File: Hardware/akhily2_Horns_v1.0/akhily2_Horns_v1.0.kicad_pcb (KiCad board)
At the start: 2 copper layers, 0 parts

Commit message: Save work before applying fixes
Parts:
- added C1: 0.1uF, Capacitor_THT:CP_Radial_D5.0mm_P2.00mm, F.Cu at (87.0, 75.0)
- added C2: 0.1uF, Capacitor_THT:CP_Radial_D5.0mm_P2.00mm, F.Cu at (99.0, 75.0)
- added C3: 0.1uF, Capacitor_THT:CP_Radial_D5.0mm_P2.00mm, F.Cu at (111.0, 75.0)
- added C4: 1uF, Capacitor_THT:CP_Radial_D5.0mm_P2.00mm, F.Cu at (123.0, 75.0)
- added C5: 1uF, Capacitor_THT:CP_Radial_D5.0mm_P2.00mm, F.Cu at (87.0, 90.0)
- added C6: 10uF, Capacitor_THT:CP_Radial_D5.0mm_P2.00mm, F.Cu at (99.0, 90.0)
- added C7: 10uF, Capacitor_THT:CP_Radial_D5.0mm_P2.00mm, F.Cu at (111.0, 90.0)
- added C8: 100uF, Capacitor_THT:CP_Radial_D5.0mm_P2.00mm, F.Cu at (123.0, 90.0)
- added C9: 0.1uF, Capacitor_THT:CP_Radial_D5.0mm_P2.00mm, F.Cu at (72.0, 87.0)
- added D1: ES2DA-13-F, Diode_THT:D_DO-41_SOD81_P10.16mm_Horizontal, F.Cu at (58.8, 100.5)
- added F1: 2A, Fuse:Fuseholder_Cylinder-5x20mm_Schurter_FAB_0031-355x_Horizontal_Closed, F.Cu at (62.0, 75.0)
- added J1: Conn_01x03, Connector_PinHeader_2.54mm:PinHeader_1x03_P2.54mm_Vertical, F.Cu at (33.5, 51.0)
- added J2: Conn_01x02, Connector_PinHeader_2.54mm:PinHeader_1x02_P2.54mm_Vertical, F.Cu at (33.5, 66.0)
- added J3: Conn_01x02, Connector_PinHeader_2.54mm:PinHeader_1x02_P2.54mm_Vertical, F.Cu at (33.5, 81.0)
- added J4: Conn_01x02, Connector_PinHeader_2.54mm:PinHeader_1x02_P2.54mm_Vertical, F.Cu at (33.5, 96.0)
- added Q1: Q_NMOS_GSD, Package_TO_SOT_SMD:TO-252-2, F.Cu at (62.0, 87.0)
- added R1: 1k, Resistor_THT:R_Axial_DIN0207_L6.3mm_D2.5mm_P10.16mm_Horizontal, F.Cu at (72.0, 75.0)
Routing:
- net +24V: track 0.00 -> 190.4 mm
- net Net-(Q1-D): track 0.00 -> 173.4 mm
- net GND: track 0.00 -> 120.3 mm
- net /HORN_CTL: track 0.00 -> 87.0 mm
- net /HORN_IN: track 0.00 -> 76.1 mm
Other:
- board outline added: 110 x 65 mm

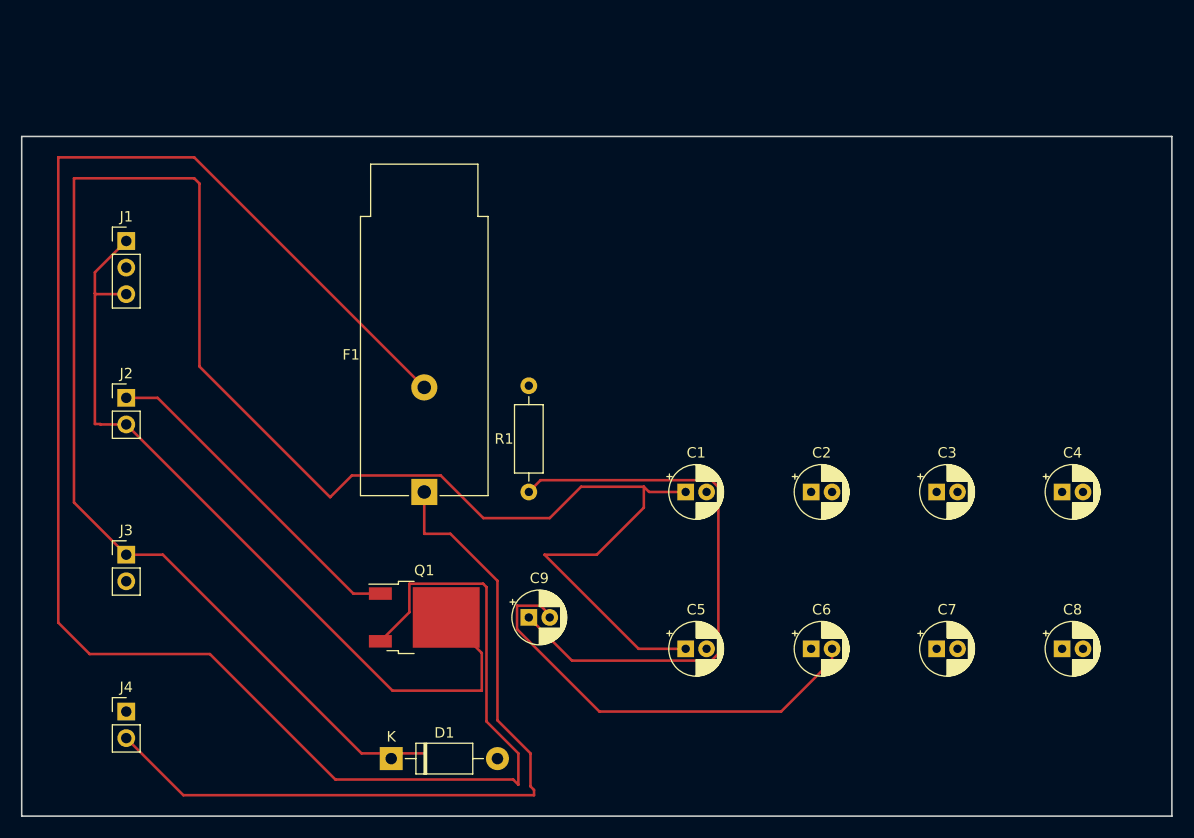
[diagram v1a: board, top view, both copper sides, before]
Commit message: Horns board specs, schematic, layout, gerbers
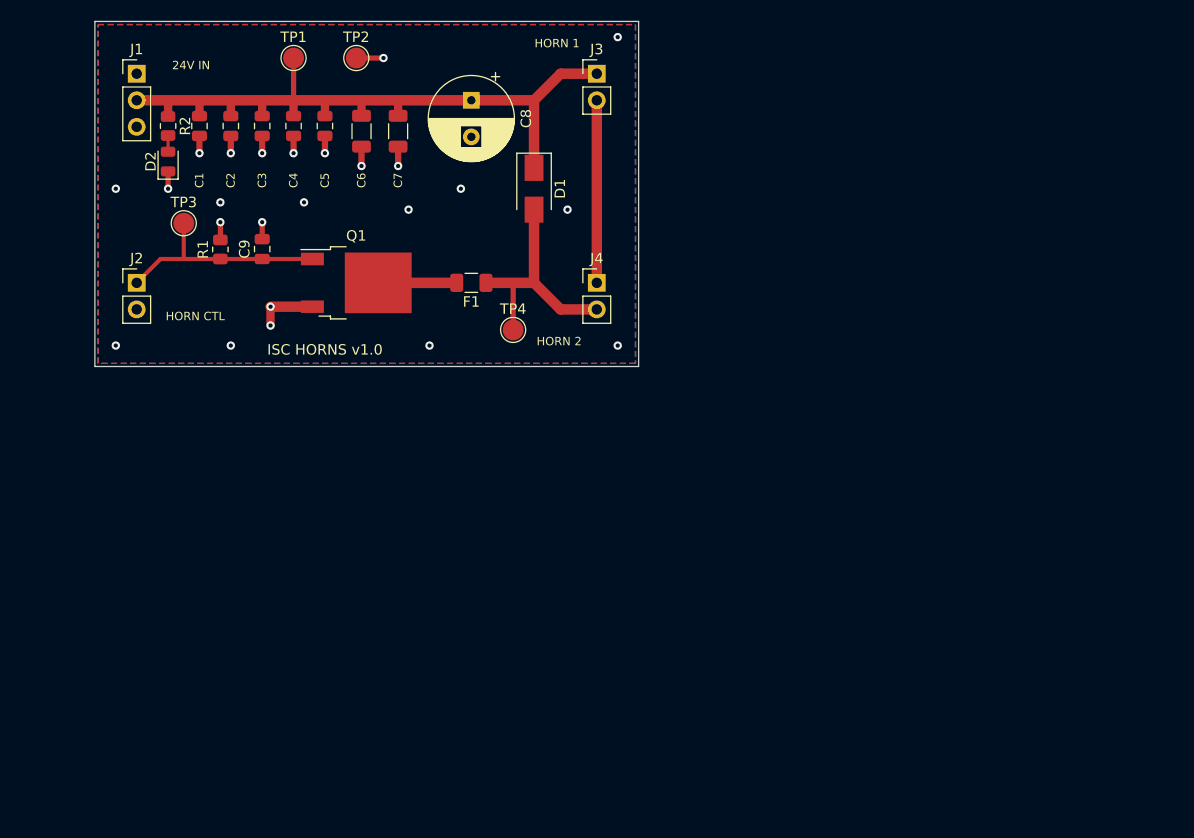
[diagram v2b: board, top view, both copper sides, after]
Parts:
- added D2: LED_GREEN, LED_SMD:LED_0805_2012Metric, F.Cu at (37.5, 43.4)
- added R2: 10k, Resistor_SMD:R_0805_2012Metric, F.Cu at (37.5, 40.0)
- added TP1: +24V, TestPoint:TestPoint_Pad_D2.0mm, F.Cu at (49.5, 33.5)
- added TP2: GND, TestPoint:TestPoint_Pad_D2.0mm, F.Cu at (55.5, 33.5)
- added TP3: HORN_CTL, TestPoint:TestPoint_Pad_D2.0mm, F.Cu at (39.0, 49.3)
- added TP4: HORN_IN, TestPoint:TestPoint_Pad_D2.0mm, F.Cu at (70.5, 59.5)
- C1, C2, C3, C9: value 0.1uF -> 0.1uF 50V; footprint Capacitor_THT:CP_Radial_D5.0mm_P2.00mm -> Capacitor_SMD:C_0805_2012Metric
- C4, C5: value 1uF -> 1uF 50V; footprint Capacitor_THT:CP_Radial_D5.0mm_P2.00mm -> Capacitor_SMD:C_0805_2012Metric
- C6, C7: value 10uF -> 10uF 50V; footprint Capacitor_THT:CP_Radial_D5.0mm_P2.00mm -> Capacitor_SMD:C_1206_3216Metric
- C8: value 100uF -> 100uF 50V; footprint Capacitor_THT:CP_Radial_D5.0mm_P2.00mm -> Capacitor_THT:CP_Radial_D8.0mm_P3.50mm
- D1: footprint Diode_THT:D_DO-41_SOD81_P10.16mm_Horizontal -> Diode_SMD:D_SMA
- F1: footprint Fuse:Fuseholder_Cylinder-5x20mm_Schurter_FAB_0031-355x_Horizontal_Closed -> Fuse:Fuse_1206_3216Metric
- Q1: value Q_NMOS_GSD -> IRFR010PBF
- R1: footprint Resistor_THT:R_Axial_DIN0207_L6.3mm_D2.5mm_P10.16mm_Horizontal -> Resistor_SMD:R_0805_2012Metric
- moved C4 81.4 mm to (49.5, 40.0), turned to -90 degrees
- moved C8 77.1 mm to (66.5, 37.5), turned to -90 degrees
- moved C3 73.4 mm to (46.5, 40.0), turned to -90 degrees
- moved C7 71.4 mm to (59.5, 40.5), turned to -90 degrees
- moved C2 65.6 mm to (43.5, 40.0), turned to -90 degrees
- moved C6 65.6 mm to (56.0, 40.5), turned to -90 degrees
- moved J3 64.4 mm to (78.5, 35.0)
- moved J4 60.9 mm to (78.5, 55.0)
- moved C5 60.7 mm to (52.5, 40.0), turned to -90 degrees
- moved C1 58.2 mm to (40.5, 40.0), turned to -90 degrees
- moved D1 56.2 mm to (72.5, 46.0), turned to -90 degrees
- moved C9 43.5 mm to (46.5, 51.8), turned to 90 degrees
- moved R1 37.5 mm to (42.5, 51.8)
- moved Q1 32.7 mm to (55.5, 55.0)
- moved F1 20.5 mm to (66.5, 55.0), turned to 180 degrees
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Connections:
- net Net-(J3-Pin_2) renamed /HORN_MID
- Q1 pad 2: GND -> Net-(Q1-D)
- Q1 pad 3: Net-(Q1-D) -> GND
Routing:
- net Net-(Q1-D): track 173.4 -> 8.34 mm
- net +24V: track 190.4 -> 67.6 mm
- net GND: track 120.3 -> 24.5 mm, vias 0 -> 24
- net /HORN_CTL: track 87.0 -> 20.3 mm
- net /HORN_IN: track 76.1 -> 23.2 mm
- net /HORN_MID: track 0.00 -> 17.5 mm
- net Net-(D2-A): track 0.00 -> 1.55 mm
- added copper zone on B.Cu, net GND
- added copper zone on F.Cu, net GND
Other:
- board size 110 x 65 mm -> 52 x 33 mm
- board text added: "24V IN"
- board text added: "HORN 1"
- board text added: "HORN 2"
- board text added: "HORN CTL"
- board text added: "ISC HORNS v1.0"
